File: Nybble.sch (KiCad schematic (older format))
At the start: 106 parts, among them J1 USB_mini_micro_B, SW1 SW_PUSH, U1 ATMEGA32U4, X1 XTAL_GND

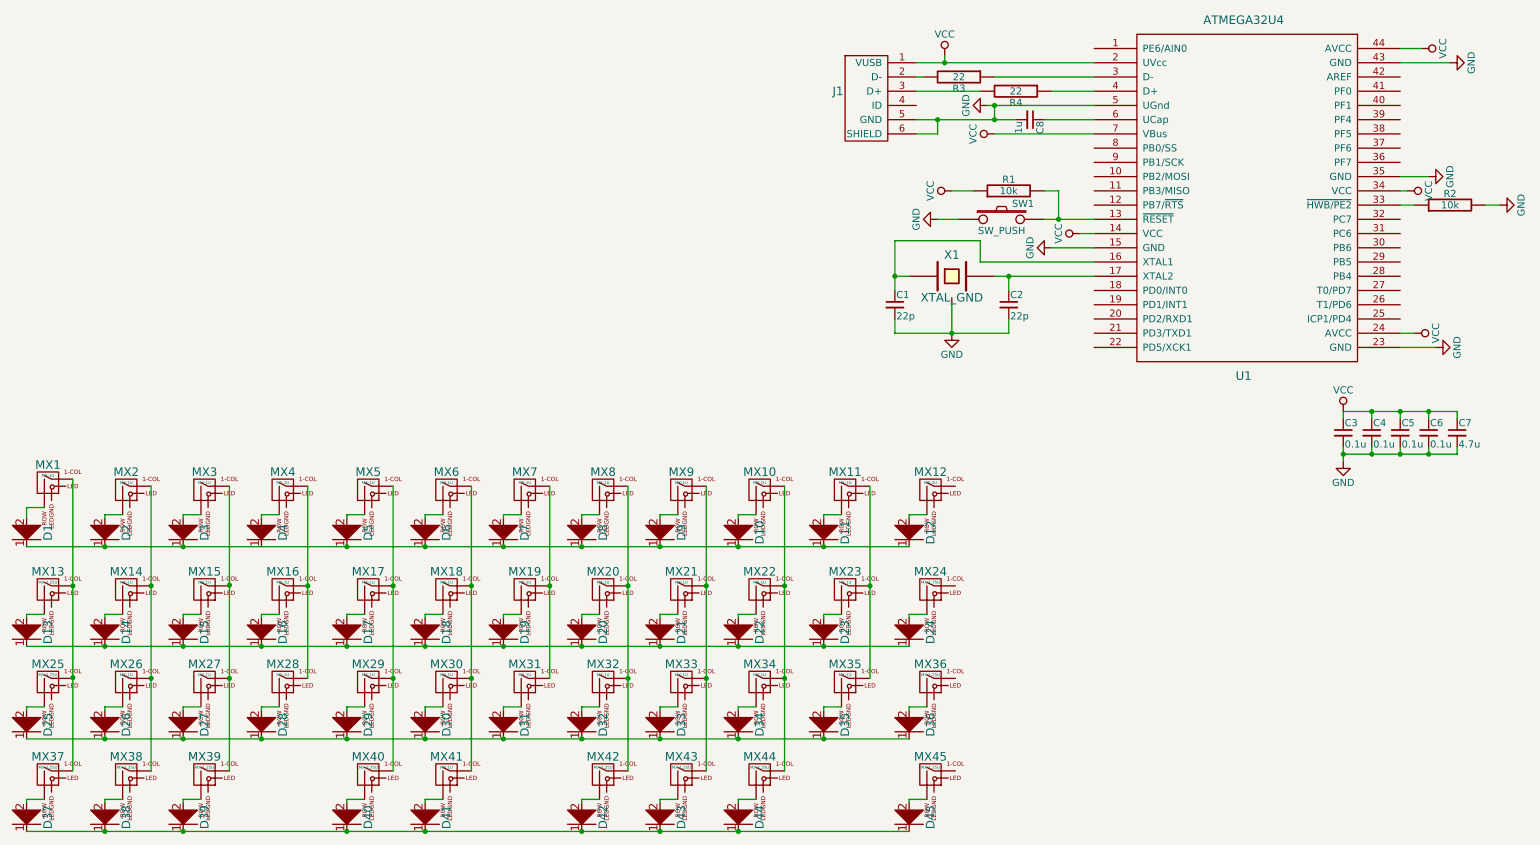
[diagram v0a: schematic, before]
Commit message: Finished the Switch Matrix -- May need to fix the labels
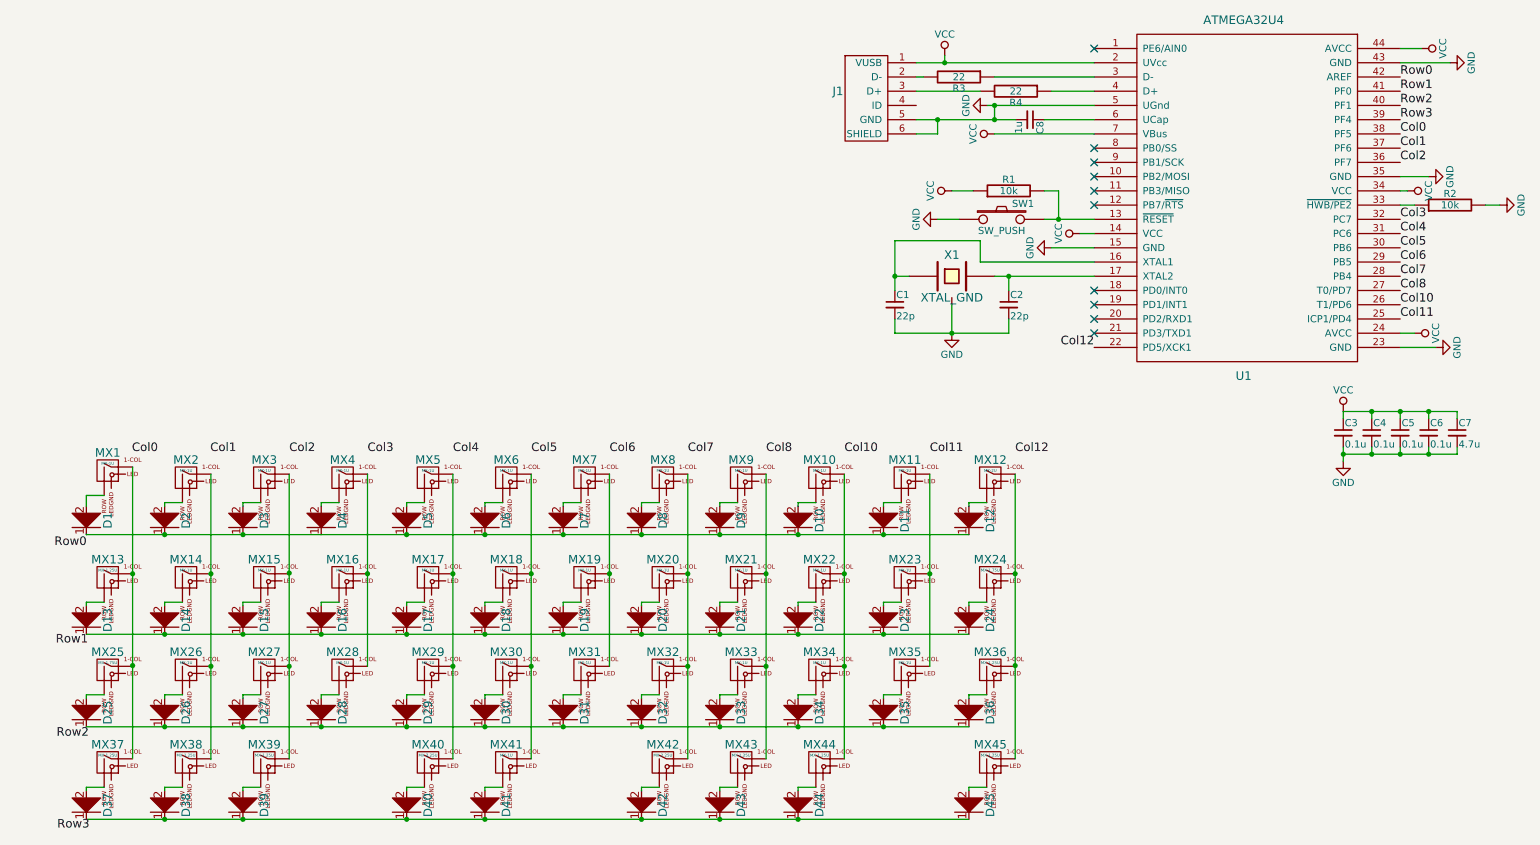
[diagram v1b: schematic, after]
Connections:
- net labels added: Col0, Col1, Col10, Col11, Col12, Col2, Col3, Col4, Col5, Col6, Col7, Col8, Row0, Row1, Row2, Row3
- wire segments 159 -> 162
- no-connect marks 0 -> 10
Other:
- moved on the sheet: D1, D10, D11, D12, D13, D14, D15, D16, D17, D18, D19, D2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

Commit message: I screwed with a tonne of footprints, and attempted to generate a netlist, currently untested
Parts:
- C1, C2, C3, C4, C5, C6, C7, C8: footprint (none) -> Capacitors_SMD:C_0805_HandSoldering
- D1, D10, D11, D12, D13, D14, D15, D16, D17, D18, D19, D2, D20, D21, D22, D23, D24, D25, D26, D27, D28, D29, D3, D30, D31, D32, D33, D34, D35, D36, D37, D38, D39, D4, D40, D41, D42, D43, D44, D45, D5, D6, D7, D8, D9: footprint (none) -> keyboard_parts:D_SOD123_axial
- J1: footprint (none) -> keyboard_parts:USB_miniB_hirose_5S8
- MX1, MX10, MX11, MX12, MX14, MX15, MX16, MX17, MX18, MX19, MX2, MX20, MX21, MX22, MX23, MX26, MX27, MX28, MX29, MX3, MX30, MX31, MX32, MX33, MX34, MX35, MX4, MX41, MX5, MX6, MX7, MX8, MX9: footprint (none) -> MX_Alps_Hybrid:ALPS-1U
- MX13, MX36, MX37, MX38, MX39, MX43, MX44, MX45: footprint (none) -> MX_Alps_Hybrid:ALPS-1.25U
- MX24, MX25: footprint (none) -> MX_Alps_Hybrid:ALPS-1.75U
- MX40, MX42: footprint (none) -> MX_Alps_Hybrid:ALPS-2.25U
- R1, R2, R3, R4: footprint (none) -> Resistors_SMD:R_0805_HandSoldering
- SW1: footprint (none) -> Buttons_Switches_SMD:SW_SPST_TL3342
- U1: footprint (none) -> Housings_QFP:TQFP-44_10x10mm_Pitch0.8mm
- X1: footprint (none) -> Crystals:Crystal_SMD_3225-4pin_3.2x2.5mm

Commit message: Fixed issues in row connection
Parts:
- MX1, MX10, MX11, MX14, MX15, MX16, MX17, MX18, MX19, MX2, MX20, MX21, MX22, MX23, MX26, MX27, MX28, MX29, MX3, MX30, MX31, MX32, MX33, MX34, MX35, MX4, MX41, MX5, MX6, MX7, MX8, MX9: footprint MX_Alps_Hybrid:ALPS-1U -> MX_Alps_Hybrid:MX-1U-NoLED
- MX12: footprint MX_Alps_Hybrid:ALPS-1U -> MX_Alps_Hybrid:MX-2U-NoLED
- MX13, MX36, MX37, MX38, MX39, MX43, MX44, MX45: footprint MX_Alps_Hybrid:ALPS-1.25U -> MX_Alps_Hybrid:MX-1.25U-NoLED
- MX24, MX25: footprint MX_Alps_Hybrid:ALPS-1.75U -> MX_Alps_Hybrid:MX-1.75U-NoLED
- MX40, MX42: footprint MX_Alps_Hybrid:ALPS-2.25U -> MX_Alps_Hybrid:MX-2.25U-NoLED
